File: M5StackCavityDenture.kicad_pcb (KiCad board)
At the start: 2 copper layers, 54 x 54 mm, 28 parts, among them J1 Conn_01x04, J2 Conn_01x08, J3 free_holes, J4 Conn_01x08, J5 Conn_01x02, U1 SP3485EN

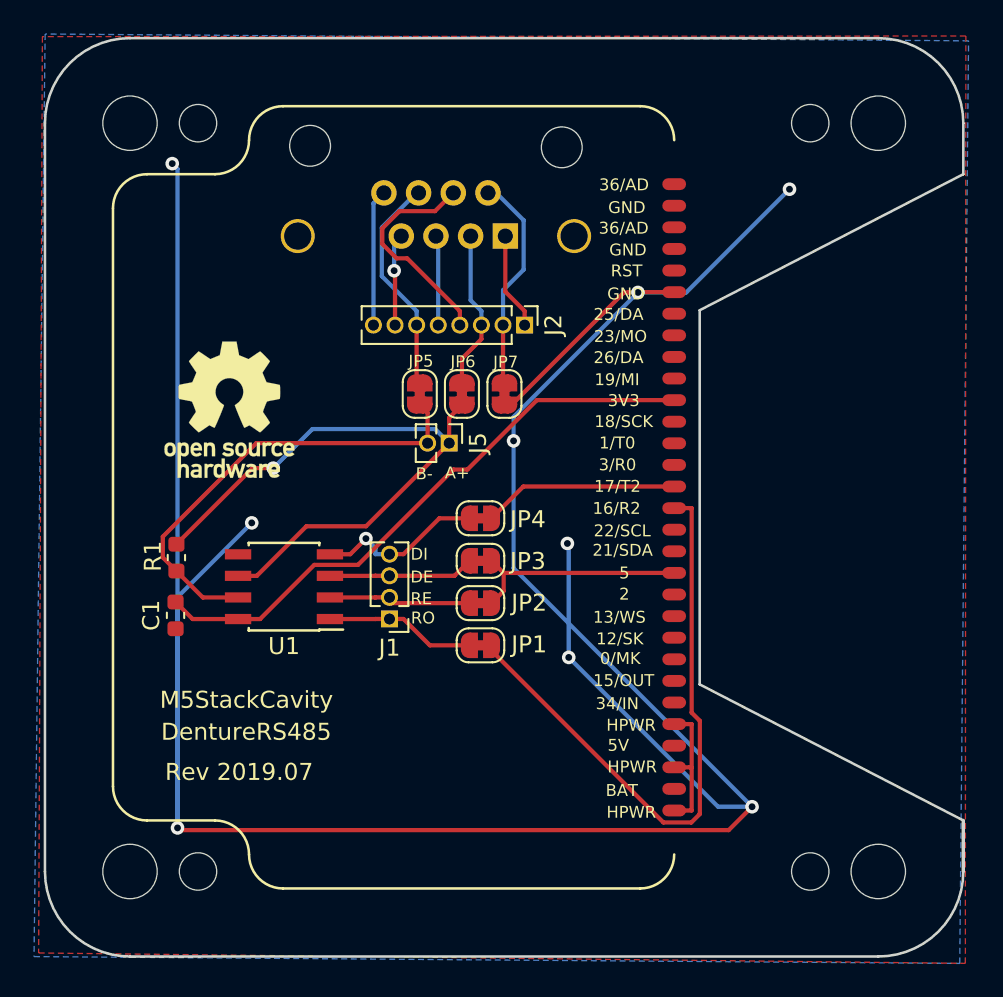
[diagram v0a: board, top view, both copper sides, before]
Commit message: Remove redundant components
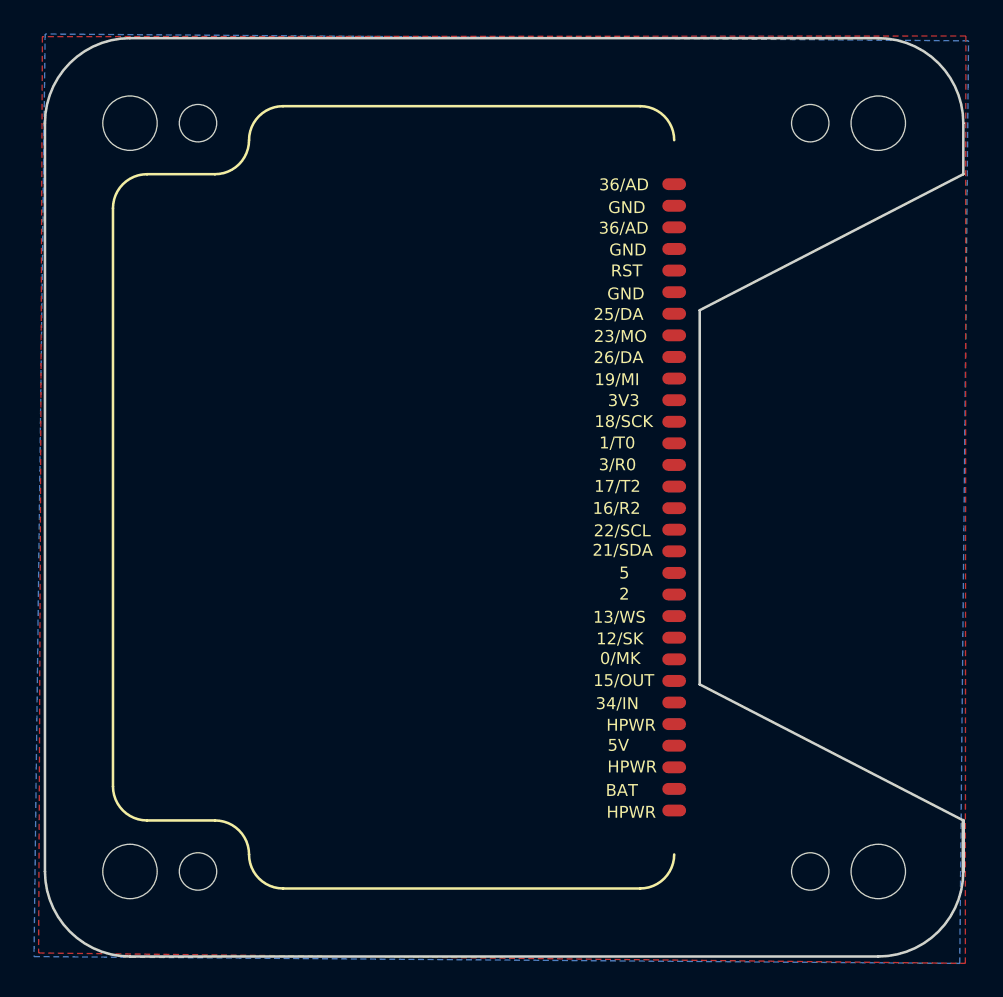
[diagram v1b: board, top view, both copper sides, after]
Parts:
- removed C1: 0.1uf, Capacitor_SMD:C_0603_1608Metric
- removed the J1 at (118.3, 82.2)
- removed J2: Conn_01x08, Connector_PinHeader_1.27mm:PinHeader_1x08_P1.27mm_Vertical
- removed J4: Conn_01x08, footprints:RJ45_Neltron_Industrial_7810-8P8C
- removed J5: Conn_01x02, Connector_PinHeader_1.27mm:PinHeader_1x02_P1.27mm_Vertical
- removed JP1, JP2, JP3, JP4, JP5, JP6, JP7: Jumper, Jumper:SolderJumper-2_P1.3mm_Bridged_RoundedPad1.0x1.5mm
- removed OSHWREF2: OSHW-Logo_7.5x8mm_SilkScreen, Symbol:OSHW-Logo_7.5x8mm_SilkScreen
- removed R1: 220, Resistor_SMD:R_0603_1608Metric
- removed U1: SP3485EN, Package_SO:SOIC-8_3.9x4.9mm_P1.27mm
- renumbered J3 to J1
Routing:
- net GND: track 177.7 -> 0.00 mm, vias 9 -> 0
- net /A+: track 37.4 -> 0.00 mm, vias 1 -> 0
- net /16: track 36.2 -> 0.00 mm
- net +3V3: track 35.1 -> 0.00 mm
- net /B-: track 26.9 -> 0.00 mm
- net /5: track 13.1 -> 0.00 mm
- net Net-(J2-Pad6): track 13.1 -> 0.00 mm
- net Net-(J2-Pad4): track 13.0 -> 0.00 mm
- net Net-(J2-Pad2): track 12.9 -> 0.00 mm
- net /17: track 11.5 -> 0.00 mm
- net Net-(J1-Pad4): track 10.0 -> 0.00 mm, vias 1 -> 0
- net Net-(J2-Pad3): track 9.37 -> 0.00 mm
- net Net-(J1-Pad1): track 8.85 -> 0.00 mm
- net Net-(J1-Pad3): track 8.57 -> 0.00 mm
- net Net-(J1-Pad2): track 8.56 -> 0.00 mm
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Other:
- board text added: "Please put components on back side."
- board text removed: "A+"
- board text removed: "B-"
- board text removed: "DE"
- board text removed: "DI"
- board text removed: "DentureRS485"
- board text removed: "M5StackCavity"
- board text removed: "RE"
- board text removed: "RO"
- board text removed: "Rev 2019.07"
